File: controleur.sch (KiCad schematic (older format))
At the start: 0 parts

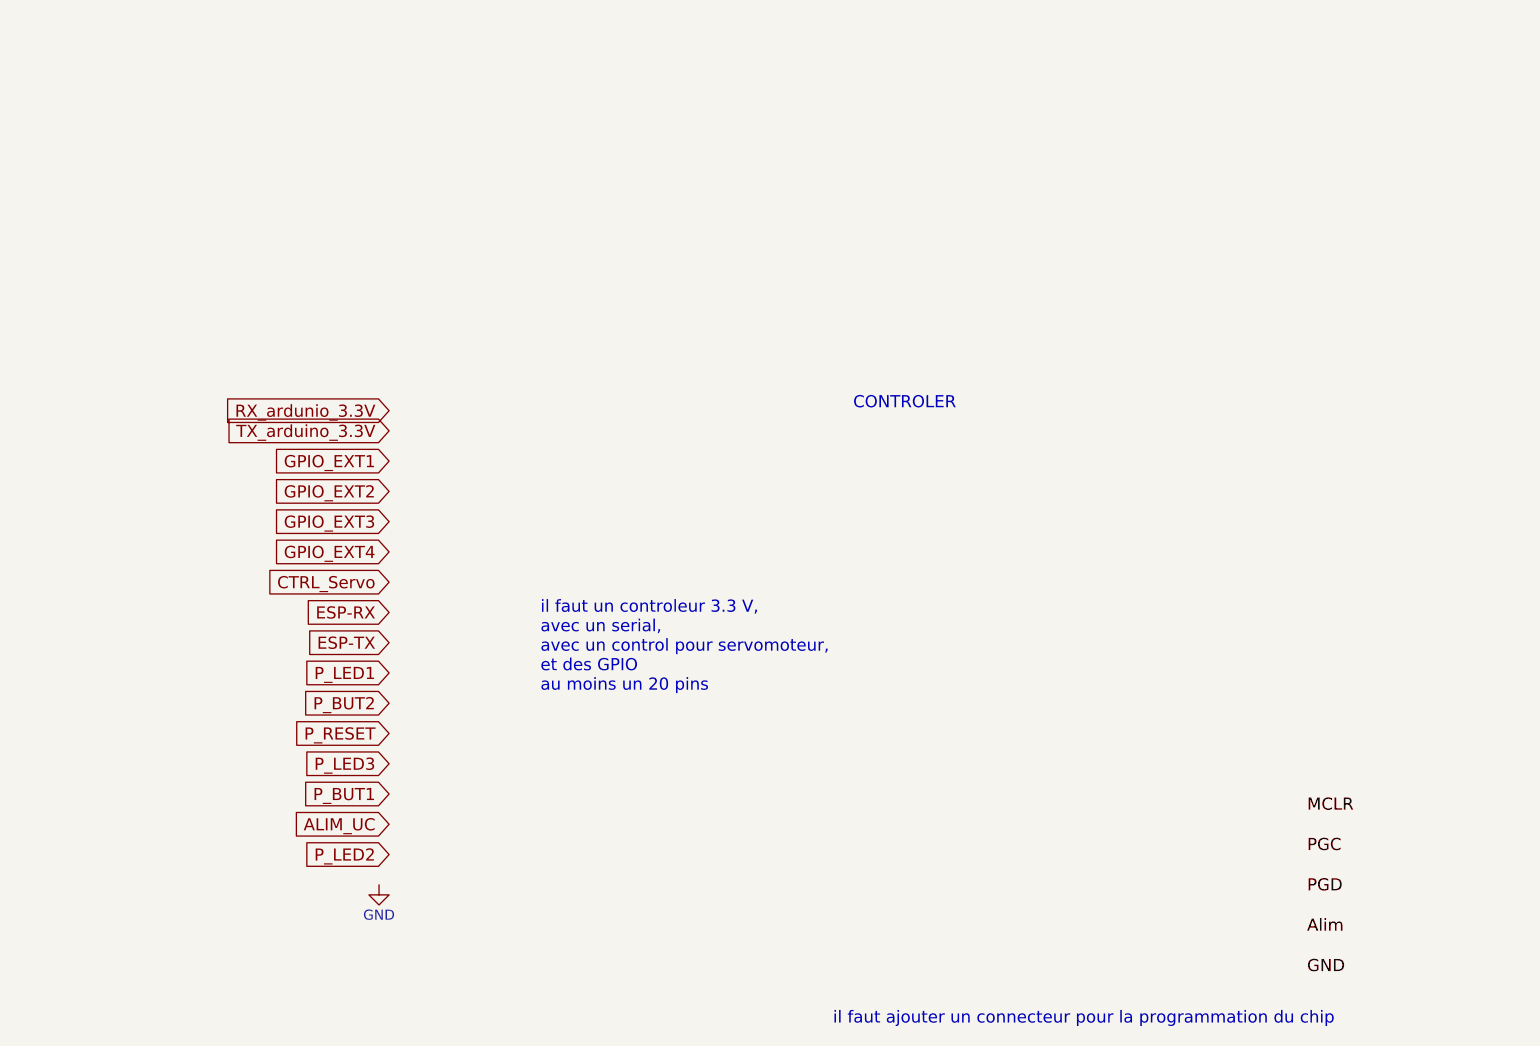
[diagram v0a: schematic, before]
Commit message: finish schematics. add componants, find right chip, firest verification OK, ready for routing
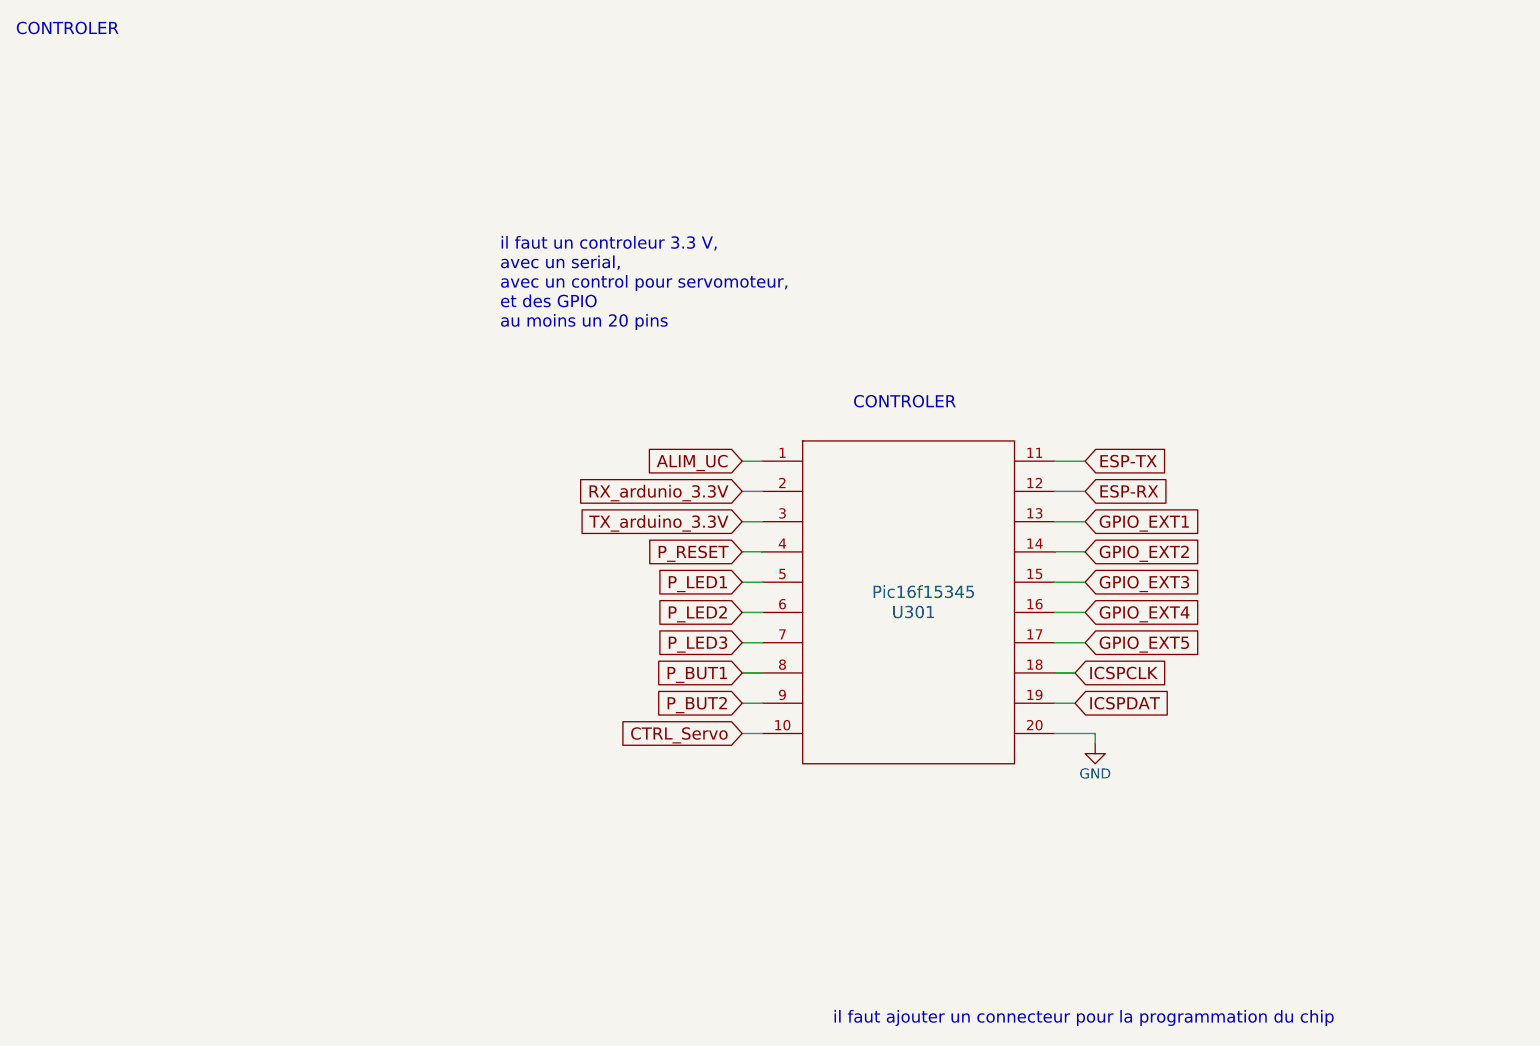
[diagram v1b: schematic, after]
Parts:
- added U301: Pic16f15345, Housings_DIP:DIP-20_W7.62mm_LongPads, symbol Pic16f15345
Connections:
- net ALIM_UC: now also U301.1
- net CTRL_Servo: now also U301.10
- net ESP-RX: now also U301.12
- net ESP-TX: now also U301.11
- net GND: now also U301.20
- net GPIO_EXT1: now also U301.13
- net GPIO_EXT2: now also U301.14
- net GPIO_EXT3: now also U301.15
- net GPIO_EXT4: now also U301.16
- net P_BUT1: now also U301.8
- net P_BUT2: now also U301.9
- net P_LED1: now also U301.5
- net P_LED2: now also U301.6
- net P_LED3: now also U301.7
- net P_RESET: now also U301.4
- net RX_ardunio_3.3V: now also U301.2
- net TX_arduino_3.3V: now also U301.3
- new net GPIO_EXT5: U301.17
- new net ICSPCLK: U301.18
- new net ICSPDAT: U301.19
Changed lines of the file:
@@
 CONTROLER
 $Comp
-L GND #PWR012
+L GND #PWR016
 U 1 1 5A7A419A
-P 3250 4450
-F 0 "#PWR012" H 3250 4200 50  0001 C CNN
-F 1 "GND" H 3250 4300 50  0000 C CNN
-F 2 "" H 3250 4450 50  0001 C CNN
-F 3 "" H 3250 4450 50  0001 C CNN
-	1    3250 4450
+P 6800 3750
+F 0 "#PWR016" H 6800 3500 50  0001 C CNN
+F 1 "GND" H 6800 3600 50  0000 C CNN
+F 2 "" H 6800 3750 50  0001 C CNN
+F 3 "" H 6800 3750 50  0001 C CNN
+	1    6800 3750
 	1    0    0    -1
 $EndComp
-Text GLabel 3300 2950 0    60   Input ~ 0
+Text GLabel 5050 3700 0    60   Input ~ 0
 CTRL_Servo
-Text GLabel 3300 3400 0    60   Input ~ 0
+Text GLabel 5050 2950 0    60   Input ~ 0
 P_LED1
-Text GLabel 3300 4300 0    60   Input ~ 0
+Text GLabel 5050 3100 0    60   Input ~ 0
 P_LED2
-Text GLabel 3300 3850 0    60   Input ~ 0
+Text GLabel 5050 3250 0    60   Input ~ 0
 P_LED3
-Text GLabel 3300 4150 0    60   Input ~ 0
+Text GLabel 5050 2350 0    60   Input ~ 0
 ALIM_UC
-Text GLabel 3300 4000 0    60   Input ~ 0
+Text GLabel 5050 3400 0    60   Input ~ 0
 P_BUT1
-Text GLabel 3300 3550 0    60   Input ~ 0
+Text GLabel 5050 3550 0    60   Input ~ 0
 P_BUT2
-Text GLabel 3300 3700 0    60   Input ~ 0
+Text GLabel 5050 2800 0    60   Input ~ 0
 P_RESET
-Text GLabel 3300 3100 0    60   Input ~ 0
+Text GLabel 6750 2500 2    60   Input ~ 0
 ESP-RX
-Text GLabel 3300 3250 0    60   Input ~ 0
+Text GLabel 6750 2350 2    60   Input ~ 0
 ESP-TX
-Text GLabel 3300 2350 0    60   Input ~ 0
+Text GLabel 6750 2650 2    60   Input ~ 0
 GPIO_EXT1
-Text GLabel 3300 2500 0    60   Input ~ 0
+Text GLabel 6750 2800 2    60   Input ~ 0
 GPIO_EXT2
-Text GLabel 3300 2650 0    60   Input ~ 0
+Text GLabel 6750 2950 2    60   Input ~ 0
 GPIO_EXT3
-Text GLabel 3300 2800 0    60   Input ~ 0
+Text GLabel 6750 3100 2    60   Input ~ 0
 GPIO_EXT4
-Text Notes 4050 3500 0    60   ~ 0
+Text Notes 3850 1700 0    60   ~ 0
 il faut un controleur 3.3 V,\navec un serial, \navec un control pour servomoteur,\net des GPIO\nau moins un 20 pins
-Text Label 7850 4100 0    60   ~ 0
-MCLR
-Text Label 7850 4300 0    60   ~ 0
-PGC
-Text Label 7850 4500 0    60   ~ 0
-PGD
-Text Label 7850 4700 0    60   ~ 0
-Alim
-Text Label 7850 4900 0    60   ~ 0
-GND
 Text Notes 5500 5150 0    60   ~ 0
 il faut ajouter un connecteur pour la programmation du chip
-Text GLabel 3300 2200 0    60   Input ~ 0
+Text GLabel 5050 2650 0    60   Input ~ 0
 TX_arduino_3.3V
-Text GLabel 3300 2100 0    60   Input ~ 0
+Text GLabel 5050 2500 0    60   Input ~ 0
 RX_ardunio_3.3V
+$Comp
+L Pic16f15345 U301
+U 1 1 5A9B27DC
+P 5900 3100
+F 0 "U301" H 5900 3100 60  0000 C CNN
+F 1 "Pic16f15345" H 5950 3200 60  0000 C CNN
+F 2 "Housings_DIP:DIP-20_W7.62mm_LongPads" H 5900 3100 60  0001 C CNN
+F 3 "" H 5900 3100 60  0001 C CNN
+	1    5900 3100
+	1    0    0    -1
+$EndComp
+Wire Wire Line
+	5050 2350 5150 2350
+Wire Wire Line
+	6800 3750 6800 3700
+Wire Wire Line
+	6800 3700 6600 3700
+Wire Wire Line
+	5050 2800 5150 2800
+Text GLabel 6700 3550 2    60   Input ~ 0
+ICSPDAT
+Wire Wire Line
+	6700 3550 6600 3550
+Text GLabel 6700 3400 2    60   Input ~ 0
+ICSPCLK
+Wire Wire Line
+	6700 3400 6600 3400
+Text Notes 1450 250  0    60   ~ 0
+CONTROLER
+Wire Wire Line
+	5050 2650 5150 2650
+Wire Wire Line
+	5050 2500 5150 2500
+Wire Wire Line
+	6600 2350 6750 2350
+Wire Wire Line
+	6600 2500 6750 2500
+Wire Wire Line
+	5050 3700 5150 3700
+Wire Wire Line
+	5050 3550 5150 3550
+Wire Wire Line
+	5050 3400 5150 3400
+Wire Wire Line
+	5050 3250 5150 3250
+Wire Wire Line
+	5050 3100 5150 3100
+Wire Wire Line
+	5050 2950 5150 2950
+Wire Wire Line
+	6600 2650 6750 2650
+Wire Wire Line
+	6600 2800 6750 2800
+Wire Wire Line
+	6600 2950 6750 2950
+Wire Wire Line
+	6600 3100 6750 3100
+Text GLabel 6750 3250 2    60   Input ~ 0
+GPIO_EXT5
+Wire Wire Line
+	6750 3250 6600 3250
 $EndSCHEMATC
